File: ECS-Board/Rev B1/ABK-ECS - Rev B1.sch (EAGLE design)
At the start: 272 parts, among them J1 USB-B-S-RA, J10 FTSH-105-01-L-DV-NOPASTE, J11 22-05-7028-02, J12 RB1-125BAG1A, J2 MSTBA2, J3 22-05-7068-06, J4 22-05-7028-02, J5 22-05-7068-06, J6 22-05-7068-06, J7 22-05-7068-06, J8 22-05-7028-02, J9 FTSH-103-01-L-DV-NOPASTE, K1 G6K-2G-Y, SW1 B3FS-1015, SW2 B3FS-1015, T1 MMBT2907ALT3, T10 MMBT2222AL, T11 IRLML5103TRPBF, T12 MMBT2222AL, T13 IRLML5103TRPBF, T14 IRLML5103TRPBF, T15 IRLML5103TRPBF, T16 IRLML5103TRPBF, T17 MMBT2222AL, T18 MMBT2222AL, T19 MMBT2222AL, T2 EXMACHINA-LOGO-NAME, T20 MMBT2222AL, T3 IRLML5103TRPBF, T4 IRLML5103TRPBF, T5 IRLML5103TRPBF, T6 IRLML5103TRPBF, T7 MMBT2222AL, T8 MMBT2222AL, T9 MMBT2222AL, U1 AT24C512C-SSHM-B, U2 LPC1768FBD100, U3 LT3686HDDPBF, U4 LT3686HDDPBF, U5 CD4050BD, U6 CD4050BD, U7 DP83848JSQ/NOPB, X1 FC-135, X2 ASE-12, X3 3000, X4 ASE_50

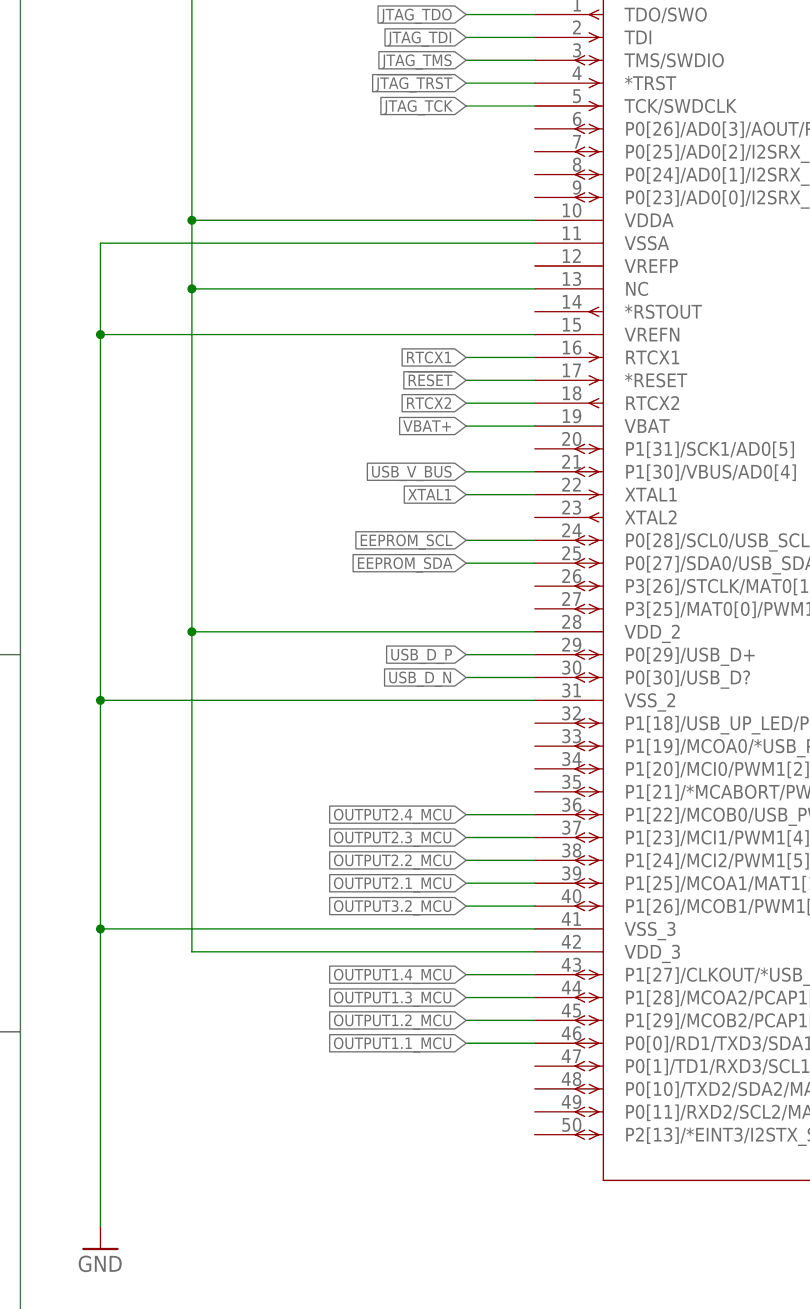
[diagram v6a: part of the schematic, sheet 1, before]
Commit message: Remape I/O and add UART-I2C-2ADC-Encoder mcu pin
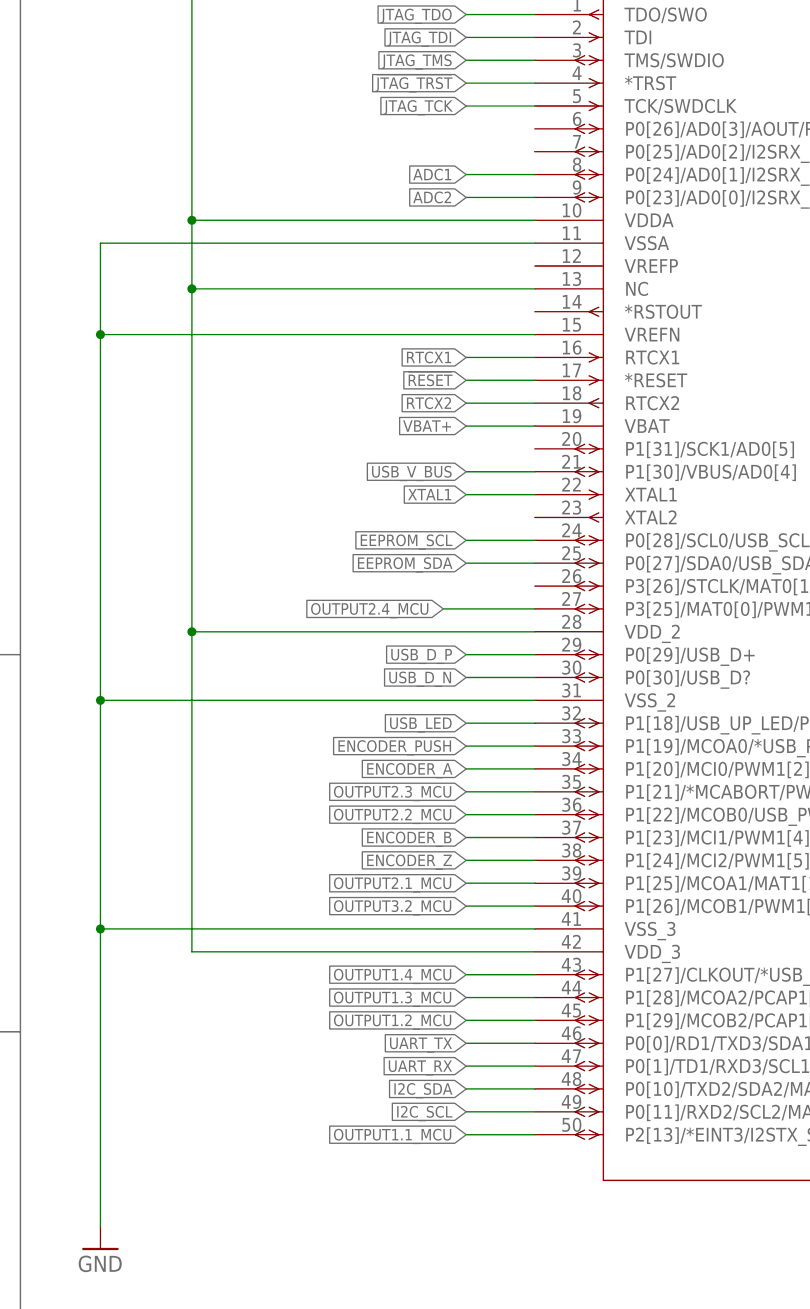
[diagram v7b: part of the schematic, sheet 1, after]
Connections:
- new net ADC1: U2.P0[24]/AD0[1]/I2SRX_WS/CAP3[1]
- new net ADC2: U2.P0[23]/AD0[0]/I2SRX_CLK/CAP3[0]
- new net ENCODER_A: U2.P1[20]/MCI0/PWM1[2]/SCK0
- new net ENCODER_B: U2.P1[23]/MCI1/PWM1[4]/MISO0
- new net ENCODER_PUSH: U2.P1[19]/MCOA0/*USB_PPWR/CAP1[1]
- new net ENCODER_Z: U2.P1[24]/MCI2/PWM1[5]/MOSI0
- new net I2C_SCL: U2.P0[11]/RXD2/SCL2/MAT3[1]
- new net I2C_SDA: U2.P0[10]/TXD2/SDA2/MAT3[0]
- new net UART_RX: U2.P0[1]/TD1/RXD3/SCL1
- new net UART_TX: U2.P0[0]/RD1/TXD3/SDA1
- new net USB_LED: U2.P1[18]/USB_UP_LED/PWM1[1]/CAP1[0]
- net OUTPUT1.1_MCU: now also U2.P2[13]/*EINT3/I2STX_SDA; no longer U2.P0[0]/RD1/TXD3/SDA1
- net OUTPUT2.2_MCU: now also U2.P1[22]/MCOB0/USB_PWRD/MAT1[0]; no longer U2.P1[24]/MCI2/PWM1[5]/MOSI0
- net OUTPUT2.3_MCU: now also U2.P1[21]/*MCABORT/PWM1[3]/SSEL0; no longer U2.P1[23]/MCI1/PWM1[4]/MISO0
- net OUTPUT2.4_MCU: now also U2.P3[25]/MAT0[0]/PWM1[2]; no longer U2.P1[22]/MCOB0/USB_PWRD/MAT1[0]
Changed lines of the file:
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@@
 <net name="OUTPUT2.3_MCU" class="0">
 <segment>
-<pinref part="U2" gate="A" pin="P1[23]/MCI1/PWM1[4]/MISO0"/>
-<wire x1="134.62" y1="142.24" x2="127" y2="142.24" width="0.1524" layer="91"/>
-<label x="127" y="142.24" size="1.27" layer="95" font="vector" ratio="10" rot="R180" xref="yes"/>
+<wire x1="134.62" y1="147.32" x2="127" y2="147.32" width="0.1524" layer="91"/>
+<label x="127" y="147.32" size="1.27" layer="95" font="vector" rot="R180" xref="yes"/>
+<pinref part="U2" gate="A" pin="P1[21]/*MCABORT/PWM1[3]/SSEL0"/>
 </segment>
 </net>
@@
 <net name="OUTPUT2.4_MCU" class="0">
 <segment>
+<wire x1="134.62" y1="167.64" x2="124.46" y2="167.64" width="0.1524" layer="91"/>
+<pinref part="U2" gate="A" pin="P3[25]/MAT0[0]/PWM1[2]"/>
+<label x="124.46" y="167.64" size="1.27" layer="95" font="vector" rot="R180" xref="yes"/>
+</segment>
+</net>
+<net name="OUTPUT2.2_MCU" class="0">
+<segment>
+<wire x1="134.62" y1="144.78" x2="127" y2="144.78" width="0.1524" layer="91"/>
+<label x="127" y="144.78" size="1.27" layer="95" font="vector" rot="R180" xref="yes"/>
 <pinref part="U2" gate="A" pin="P1[22]/MCOB0/USB_PWRD/MAT1[0]"/>
-<wire x1="134.62" y1="144.78" x2="127" y2="144.78" width="0.1524" layer="91"/>
-<label x="127" y="144.78" size="1.27" layer="95" font="vector" ratio="10" rot="R180" xref="yes"/>
-</segment>
-</net>
-<net name="OUTPUT2.2_MCU" class="0">
-<segment>
-<pinref part="U2" gate="A" pin="P1[24]/MCI2/PWM1[5]/MOSI0"/>
-<wire x1="134.62" y1="139.7" x2="127" y2="139.7" width="0.1524" layer="91"/>
-<label x="127" y="139.7" size="1.27" layer="95" font="vector" ratio="10" rot="R180" xref="yes"/>
 </segment>
 </net>
@@
 <net name="OUTPUT1.1_MCU" class="0">
 <segment>
-<pinref part="U2" gate="A" pin="P0[0]/RD1/TXD3/SDA1"/>
-<wire x1="127" y1="119.38" x2="134.62" y2="119.38" width="0.1524" layer="91"/>
-<label x="127" y="119.38" size="1.27" layer="95" font="vector" rot="R180" xref="yes"/>
+<wire x1="127" y1="109.22" x2="134.62" y2="109.22" width="0.1524" layer="91"/>
+<pinref part="U2" gate="A" pin="P2[13]/*EINT3/I2STX_SDA"/>
+<label x="127" y="109.22" size="1.27" layer="95" font="vector" rot="R180" xref="yes"/>
 </segment>
 </net>
@@
 </segment>
 </net>
+<net name="ADC2" class="0">
+<segment>
+<pinref part="U2" gate="A" pin="P0[23]/AD0[0]/I2SRX_CLK/CAP3[0]"/>
+<wire x1="134.62" y1="213.36" x2="127" y2="213.36" width="0.1524" layer="91"/>
+<label x="127" y="213.36" size="1.27" layer="95" font="vector" rot="R180" xref="yes"/>
+</segment>
+</net>
+<net name="ADC1" class="0">
+<segment>
+<pinref part="U2" gate="A" pin="P0[24]/AD0[1]/I2SRX_WS/CAP3[1]"/>
+<wire x1="134.62" y1="215.9" x2="127" y2="215.9" width="0.1524" layer="91"/>
+<label x="127" y="215.9" size="1.27" layer="95" font="vector" rot="R180" xref="yes"/>
+</segment>
+</net>
+<net name="UART_TX" class="0">
+<segment>
+<pinref part="U2" gate="A" pin="P0[0]/RD1/TXD3/SDA1"/>
+<wire x1="134.62" y1="119.38" x2="127" y2="119.38" width="0.1524" layer="91"/>
+<label x="127" y="119.38" size="1.27" layer="95" font="vector" rot="R180" xref="yes"/>
+</segment>
+</net>
+<net name="UART_RX" class="0">
+<segment>
+<pinref part="U2" gate="A" pin="P0[1]/TD1/RXD3/SCL1"/>
+<wire x1="134.62" y1="116.84" x2="127" y2="116.84" width="0.1524" layer="91"/>
+<label x="127" y="116.84" size="1.27" layer="95" font="vector" rot="R180" xref="yes"/>
+</segment>
+</net>
+<net name="I2C_SDA" class="0">
+<segment>
+<pinref part="U2" gate="A" pin="P0[10]/TXD2/SDA2/MAT3[0]"/>
+<wire x1="134.62" y1="114.3" x2="127" y2="114.3" width="0.1524" layer="91"/>
+<label x="127" y="114.3" size="1.27" layer="95" font="vector" rot="R180" xref="yes"/>
+</segment>
+</net>
+<net name="I2C_SCL" class="0">
+<segment>
+<pinref part="U2" gate="A" pin="P0[11]/RXD2/SCL2/MAT3[1]"/>
+<wire x1="134.62" y1="111.76" x2="127" y2="111.76" width="0.1524" layer="91"/>
+<label x="127" y="111.76" size="1.27" layer="95" font="vector" rot="R180" xref="yes"/>
+</segment>
+</net>
+<net name="USB_LED" class="0">
+<segment>
+<pinref part="U2" gate="A" pin="P1[18]/USB_UP_LED/PWM1[1]/CAP1[0]"/>
+<wire x1="134.62" y1="154.94" x2="127" y2="154.94" width="0.1524" layer="91"/>
+<label x="127" y="154.94" size="1.27" layer="95" font="vector" rot="R180" xref="yes"/>
+</segment>
+</net>
+<net name="ENCODER_A" class="0">
+<segment>
+<pinref part="U2" gate="A" pin="P1[20]/MCI0/PWM1[2]/SCK0"/>
+<wire x1="134.62" y1="149.86" x2="127" y2="149.86" width="0.1524" layer="91"/>
+<label x="127" y="149.86" size="1.27" layer="95" font="vector" rot="R180" xref="yes"/>
+</segment>
+</net>
+<net name="ENCODER_B" class="0">
+<segment>
+<pinref part="U2" gate="A" pin="P1[23]/MCI1/PWM1[4]/MISO0"/>
+<wire x1="134.62" y1="142.24" x2="127" y2="142.24" width="0.1524" layer="91"/>
+<label x="127" y="142.24" size="1.27" layer="95" font="vector" rot="R180" xref="yes"/>
+</segment>
+</net>
+<net name="ENCODER_Z" class="0">
+<segment>
+<pinref part="U2" gate="A" pin="P1[24]/MCI2/PWM1[5]/MOSI0"/>
+<wire x1="134.62" y1="139.7" x2="127" y2="139.7" width="0.1524" layer="91"/>
+<label x="127" y="139.7" size="1.27" layer="95" font="vector" rot="R180" xref="yes"/>
+</segment>
+</net>
+<net name="ENCODER_PUSH" class="0">
+<segment>
+<pinref part="U2" gate="A" pin="P1[19]/MCOA0/*USB_PPWR/CAP1[1]"/>
+<wire x1="134.62" y1="152.4" x2="127" y2="152.4" width="0.1524" layer="91"/>
+<label x="127" y="152.4" size="1.27" layer="95" font="vector" rot="R180" xref="yes"/>
+</segment>
+</net>

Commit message: dd pull up and pull down resistor to I2C and UART and place every compoment
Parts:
- added C35, C36: 0.1uF, rcl:C-EUC0603
- added J13: 22-05-7068-06, con-molex:22-05-7068-06
- added J14, J15, J16: 22-05-7048-04, con-molex:22-05-7048-04
- added R133, R135, R138, R139: 4K7, rcl:R-EU_R0603
- added R134, R136, R137, R140, R141, R142, R143, R144, R145, R146, R147, R148, R149, R150, R151, R152, R153, R154: 1K, rcl:R-EU_R0603
- added U10, U9: SN74LVC2G17DBVR, ti:SN74LVC2G17DBVR
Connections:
- new net N$117: J13-5.S, R133.2, R134.1
- new net N$118: J13-4.S, R136.1, R138.2
- new net N$119: J13-3.S, R135.2, R137.1
- new net N$120: R140.2, U10.2A
- new net N$121: R136.2, U9.2A
- new net N$122: R134.2, U9.1A
- new net N$123: R137.2, U10.1A
- new net N$124: J13-2.S, R139.2, R140.1
- new net N$125: J14-2.S, R141.1
- new net N$126: J14-3.S, R142.1
- new net N$127: J15-2.S, R143.1
- new net N$128: J15-3.S, R144.1
- new net N$129: J16-2.S, R145.1
- new net N$130: J16-3.S, R146.1
- net +3V3: now also C35.1, C36.1, J15-1.S, J16-1.S, R149.1, R150.1, R153.1, R154.1, U10.VCC, U9.VCC
- net +5V: now also J13-6.S, R133.1, R135.1, R138.1, R139.1
- net ADC1: now also R141.2
- net ADC2: now also R142.2
- net ENCODER_A: now also U9.1Y
- net ENCODER_B: now also U9.2Y
- net ENCODER_PUSH: now also U10.2Y
- net ENCODER_Z: now also U10.1Y
- net GND: now also C35.2, C36.2, J13-1.S, J14-4.S, J15-4.S, J16-4.S, R147.1, R148.1, R151.1, R152.1, U10.GND, U9.GND
- net I2C_SCL: now also R144.2, R148.2, R150.2
- net I2C_SDA: now also R143.2, R147.2, R149.2
- net UART_RX: now also R146.2, R152.2, R154.2
- net UART_TX: now also R145.2, R151.2, R153.2
